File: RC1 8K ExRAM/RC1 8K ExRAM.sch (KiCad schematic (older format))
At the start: 32 parts, among them J1 Expansion, J2 ADDRESS, U1 74LS138, U2 74LS00, U3 74HC595, U4 74HC595, U5 HM62256BLP-7, U6 74LS244, U7 74LS244, U8 74LS245

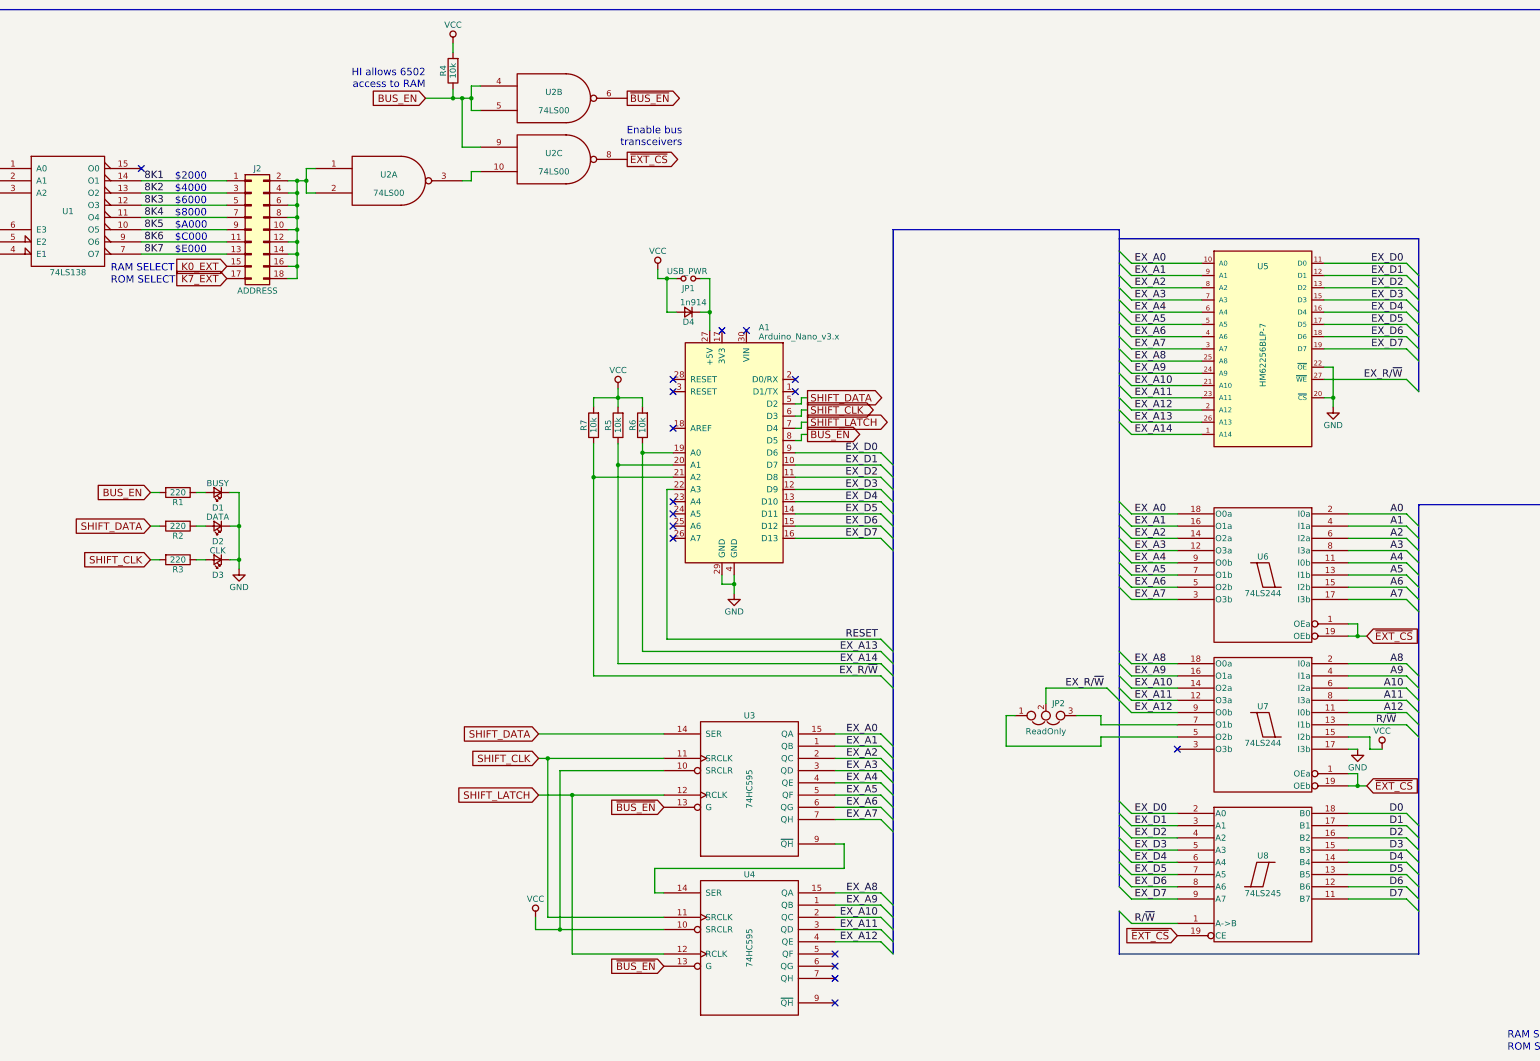
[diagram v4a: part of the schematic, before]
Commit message: Tweak ExRAM signalling
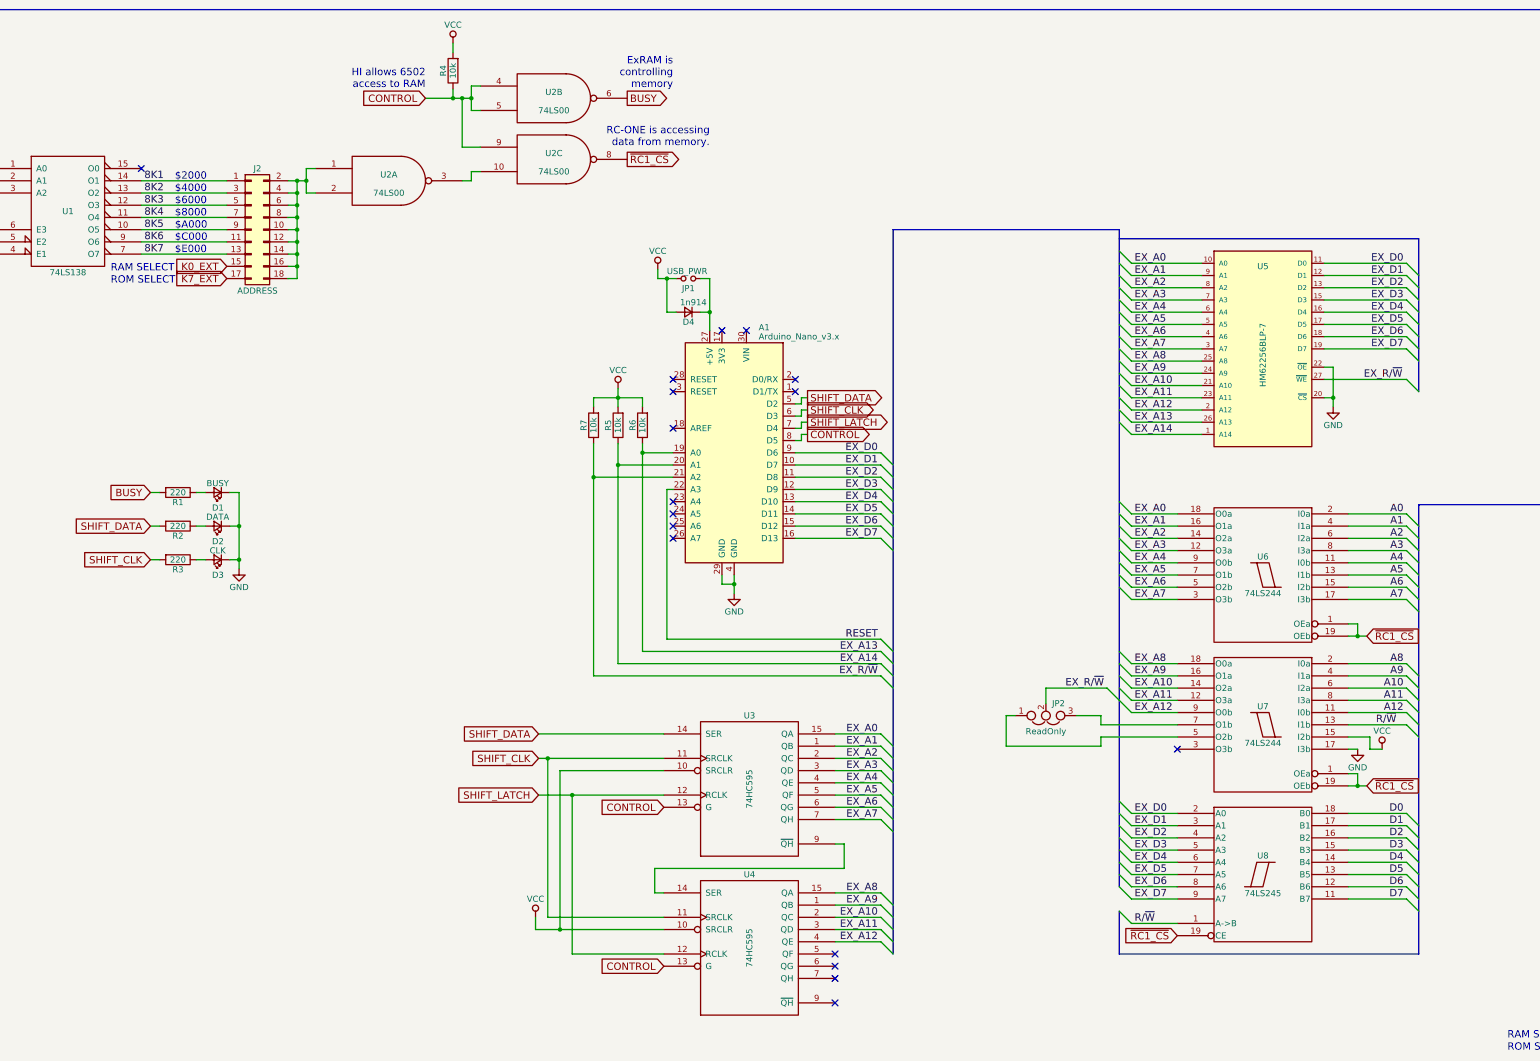
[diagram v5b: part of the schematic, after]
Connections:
- net BUS_EN renamed CONTROL
- net CONTROL: now also U3.13 (G), U4.13 (G); no longer R1.2
- removed net ~BUS_EN: U2.6, U3.13 (G), U4.13 (G)
- net ~EXT_CS renamed ~RC1_CS
- new net BUSY: R1.2, U2.6
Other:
- note added: "ExRAM is\ncontrolling\nmemory"
- note added: "RC-ONE is accessing\ndata from memory."
- note removed: "Enable bus\ntransceivers"
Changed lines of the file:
@@
 $EndComp
 Text GLabel 4850 1325 0    60   Input ~ 0
-BUS_EN
+CONTROL
 Wire Wire Line
 	14150 7150 14150 6975
@@
 	10525 7975 10625 8075
 Text GLabel 6500 1825 2    60   Output ~ 0
-~EXT_CS
+~RC1_CS
 Wire Bus Line
 	10525 7975 10525 8325
@@
 NoConn ~ 11000 6650
 Text GLabel 11000 8175 0    60   Input ~ 0
-~EXT_CS
+~RC1_CS
 Text GLabel 12550 5725 2    60   Input ~ 0
-~EXT_CS
+~RC1_CS
 Text GLabel 12550 6950 2    60   Input ~ 0
-~EXT_CS
+~RC1_CS
 Wire Wire Line
 	12200 3525 12275 3525
@@
 Wire Wire Line
 	10625 2875 11200 2875
-Text Notes 6950 1725 2    60   ~ 0
-Enable bus\ntransceivers
+Text Notes 7175 1725 2    60   ~ 0
+RC-ONE is accessing\ndata from memory.
 $Comp
 L 74HC595 U3
@@
 NoConn ~ 8200 8425
 Text GLabel 6500 1325 2    60   Output ~ 0
-~BUS_EN
+BUSY
 Wire Wire Line
 	5225 1225 5300 1225
-Text GLabel 6800 8425 0    60   Input ~ 0
-~BUS_EN
-Text GLabel 6800 7125 0    60   Input ~ 0
-~BUS_EN
 Wire Wire Line
 	5775 7025 6800 7025
@@
 NoConn ~ 7875 3725
 Text GLabel 7975 4075 2    60   Output ~ 0
-BUS_EN
+CONTROL
 Wire Wire Line
 	7275 5225 7275 5300
@@
 	7875 4925 8575 4925
 Text GLabel 2600 4550 0    60   Input ~ 0
-BUS_EN
+BUSY
 Text Label 12625 6450 0    60   ~ 0
 R/~W
@@
 	6825 4525 6875 4525
 NoConn ~ 6875 4925
+Text GLabel 6800 7125 0    60   Input ~ 0
+CONTROL
+Text GLabel 6800 8425 0    60   Input ~ 0
+CONTROL
+Text Notes 6875 1250 2    60   ~ 0
+ExRAM is\ncontrolling\nmemory
 $EndSCHEMATC
